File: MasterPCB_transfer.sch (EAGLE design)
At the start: 1070 parts, among them IC1 NCS21911SN2T1G, IC10 LDL1117S33R, IC11 LTC4222CUH#PBF, IC12 LTC4222CUH#PBF, IC13 LTC4222CUH#PBF, IC14 LTC4222CUH#PBF, IC15 LTC4222CUH#PBF, IC16 LTC4222CUH#PBF, IC17 LTC4222CUH#PBF, IC18 LTC4222CUH#PBF, IC19 LTC4222CUH#PBF, IC2 NCS21911SN2T1G, IC20 LTC4222CUH#PBF, IC21 LTC4222CUH#PBF, IC22 LTC4222CUH#PBF, IC23 LTC4222CUH#PBF, IC24 NCS21911SN2T1G, IC25 NCS21911SN2T1G, IC26 NCS21911SN2T1G, IC27 NCS21911SN2T1G, IC28 NCS21911SN2T1G, IC29 NCS21911SN2T1G, IC3 NCS21911SN2T1G, IC30 NCS21911SN2T1G, IC31 ADIS16500AMLZ, IC32 LTC6820IUD#PBF, IC33 CBTL01023GM,115, IC34 MAX889TESA+, IC35 NCS21911SN2T1G, IC36 NCS21911SN2T1G, IC37 NCS21911SN2T1G, IC38 ADS8588HIPM, IC39 NCS21911SN2T1G, IC4 LTC4222CUH#PBF, IC40 NCS21911SN2T1G, IC41 NCS21911SN2T1G, IC42 NCS21911SN2T1G, IC43 NCS21911SN2T1G, IC44 NCS21911SN2T1G, IC45 NCS21911SN2T1G, IC46 NCS21911SN2T1G, IC47 NCS21911SN2T1G, IC48 NCS21911SN2T1G, IC49 NCS21911SN2T1G, IC5 LP38692SDX-5.0_NOPB, IC50 NCS21911SN2T1G, IC51 ADS8588HIPM, IC52 ADS8588HIPM, IC53 NCS21911SN2T1G, IC54 NCS21911SN2T1G, IC55 NCS21911SN2T1G, IC56 NCS21911SN2T1G, IC57 NCS21911SN2T1G, IC58 NCS21911SN2T1G, IC59 NCS21911SN2T1G, IC6 LP38692SDX-5.0_NOPB, IC60 NCS21911SN2T1G, IC61 NCS21911SN2T1G, IC62 NCS21911SN2T1G, IC63 NCS21911SN2T1G, IC64 NCS21911SN2T1G, IC65 NCS21911SN2T1G, IC66 NCS21911SN2T1G, IC67 NCS21911SN2T1G, IC68 NCS21911SN2T1G, IC69 NCS21911SN2T1G, IC7 LDL1117S33R, IC70 NCS21911SN2T1G, IC71 NCS21911SN2T1G, IC72 NCS21911SN2T1G, IC73 NCS21911SN2T1G, IC74 NCS21911SN2T1G, IC75 NCS21911SN2T1G, IC76 NCS21911SN2T1G, IC77 NCS21911SN2T1G, IC78 NCS21911SN2T1G, IC79 NCS21911SN2T1G, IC8 LDL1117S33R, IC9 LP38692SDX-5.0_NOPB, J1 SAMTEC-SMM-104-02-X-DJ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

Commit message: Save point
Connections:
- removed net N$43: J4.18
- removed net N$46: J4.20
- net ISO_SPI_CH_SEL: now also J4.18
- net ISO_SPI_HIGH_Z_SWITCH: now also J4.20
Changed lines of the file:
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@@
 <wire x1="236.22" y1="-17.78" x2="241.3" y2="-17.78" width="0.1524" layer="94"/>
 <wire x1="241.3" y1="-17.78" x2="241.3" y2="-33.02" width="0.1524" layer="94"/>
-<wire x1="241.3" y1="-43.18" x2="236.22" y2="-43.18" width="0.1524" layer="94"/>
+<wire x1="241.3" y1="-38.1" x2="236.22" y2="-38.1" width="0.1524" layer="94"/>
 <text x="243.84" y="-30.48" size="1.778" layer="97">Flash interface</text>
-<wire x1="241.3" y1="-43.18" x2="241.3" y2="-55.88" width="0.1524" layer="94"/>
+<wire x1="241.3" y1="-38.1" x2="241.3" y2="-55.88" width="0.1524" layer="94"/>
 <wire x1="241.3" y1="-55.88" x2="236.22" y2="-55.88" width="0.1524" layer="94"/>
 <text x="243.84" y="-50.8" size="1.778" layer="97">ISO SPI link interface</text>
@@
 </segment>
 </net>
-<net name="N$43" class="0">
+<net name="ISO_SPI_CH_SEL" class="0">
 <segment>
 <pinref part="J4" gate="G$1" pin="18"/>
 <wire x1="205.74" y1="-40.64" x2="203.2" y2="-40.64" width="0.1524" layer="91"/>
-</segment>
-</net>
-<net name="N$46" class="0">
+<label x="208.28" y="-40.64" size="1.778" layer="95"/>
+</segment>
+</net>
+<net name="ISO_SPI_HIGH_Z_SWITCH" class="0">
 <segment>
 <pinref part="J4" gate="G$1" pin="20"/>
 <wire x1="205.74" y1="-43.18" x2="203.2" y2="-43.18" width="0.1524" layer="91"/>
-</segment>
-</net>
+<label x="208.28" y="-43.18" size="1.778" layer="95"/>
+</segment>
+</net>

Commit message: Night check point
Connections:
- removed net 12V: C33.1, C34.1, C35.1, IC1.VDD, IC2.VDD, IC3.VDD
- net 13.5V_BUS: now also C33.1, C34.1, C35.1, IC1.VDD, IC2.VDD, IC3.VDD
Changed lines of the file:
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@@
-</segment>
-</net>
-<net name="12V" class="0">
-<segment>
-<pinref part="IC1" gate="G$1" pin="VDD"/>
-<wire x1="289.56" y1="218.44" x2="294.64" y2="218.44" width="0.1524" layer="91"/>
-<label x="294.64" y="218.44" size="1.778" layer="95"/>
-<pinref part="C33" gate="G$1" pin="1"/>
-<wire x1="294.64" y1="218.44" x2="294.64" y2="215.9" width="0.1524" layer="91"/>
-</segment>
-<segment>
-<pinref part="IC2" gate="G$1" pin="VDD"/>
-<wire x1="289.56" y1="177.8" x2="294.64" y2="177.8" width="0.1524" layer="91"/>
-<label x="294.64" y="177.8" size="1.778" layer="95"/>
-<pinref part="C34" gate="G$1" pin="1"/>
-<wire x1="294.64" y1="177.8" x2="294.64" y2="175.26" width="0.1524" layer="91"/>
-</segment>
-<segment>
-<pinref part="IC3" gate="G$1" pin="VDD"/>
-<wire x1="289.56" y1="137.16" x2="294.64" y2="137.16" width="0.1524" layer="91"/>
-<label x="294.64" y="137.16" size="1.778" layer="95"/>
-<pinref part="C35" gate="G$1" pin="1"/>
-<wire x1="294.64" y1="137.16" x2="294.64" y2="134.62" width="0.1524" layer="91"/>
 </segment>
 </net>
@@
 </segment>
 </net>
+<net name="13.5V_BUS" class="0">
+<segment>
+<pinref part="IC1" gate="G$1" pin="VDD"/>
+<wire x1="289.56" y1="218.44" x2="294.64" y2="218.44" width="0.1524" layer="91"/>
+<label x="294.64" y="218.44" size="1.778" layer="95"/>
+<pinref part="C33" gate="G$1" pin="1"/>
+<wire x1="294.64" y1="218.44" x2="294.64" y2="215.9" width="0.1524" layer="91"/>
+</segment>
+<segment>
+<pinref part="IC2" gate="G$1" pin="VDD"/>
+<wire x1="289.56" y1="177.8" x2="294.64" y2="177.8" width="0.1524" layer="91"/>
+<label x="294.64" y="177.8" size="1.778" layer="95"/>
+<pinref part="C34" gate="G$1" pin="1"/>
+<wire x1="294.64" y1="177.8" x2="294.64" y2="175.26" width="0.1524" layer="91"/>
+</segment>
+<segment>
+<pinref part="IC3" gate="G$1" pin="VDD"/>
+<wire x1="289.56" y1="137.16" x2="294.64" y2="137.16" width="0.1524" layer="91"/>
+<label x="294.64" y="137.16" size="1.778" layer="95"/>
+<pinref part="C35" gate="G$1" pin="1"/>
+<wire x1="294.64" y1="137.16" x2="294.64" y2="134.62" width="0.1524" layer="91"/>
+</segment>
+</net>

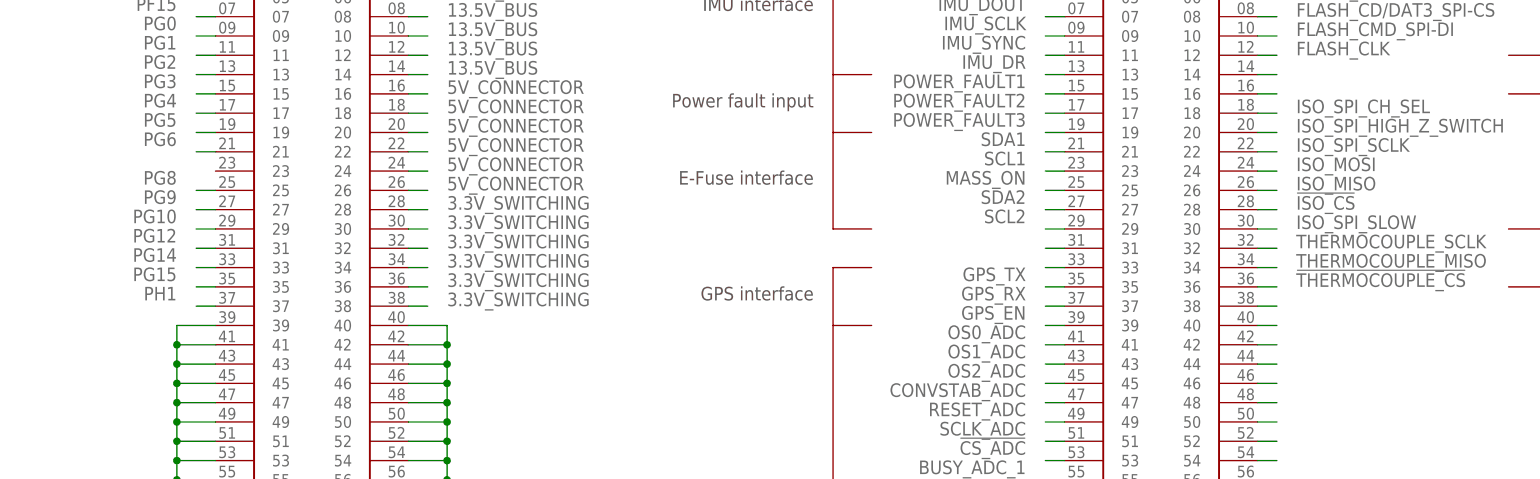
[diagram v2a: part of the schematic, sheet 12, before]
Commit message: Checked warnings on schematic, connected 40G input pin
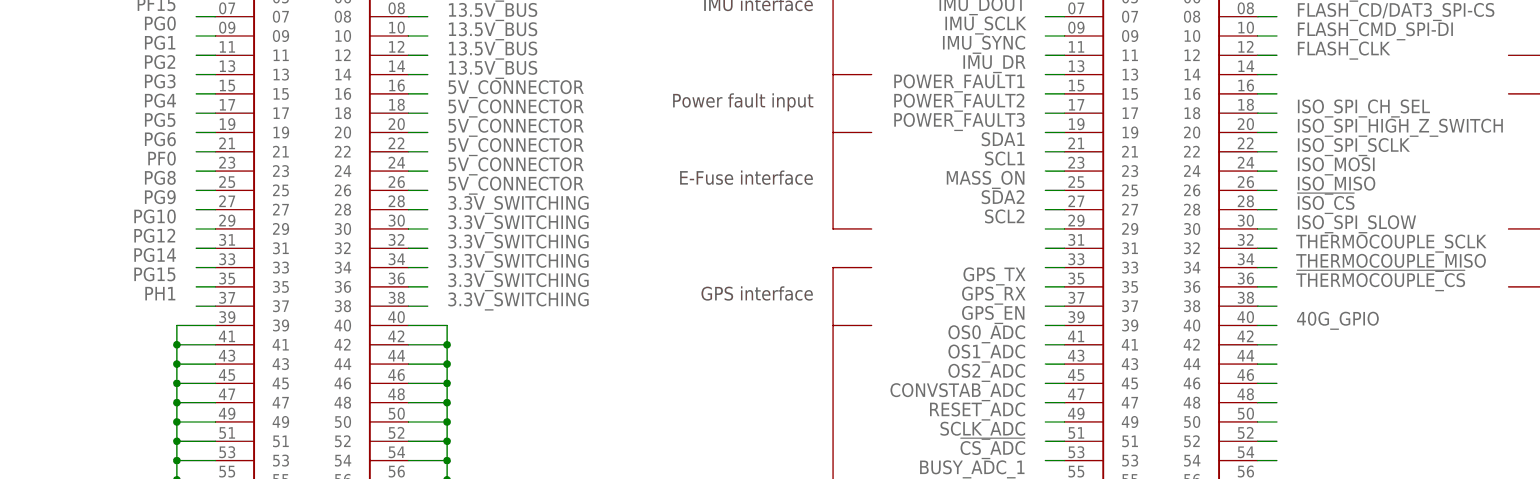
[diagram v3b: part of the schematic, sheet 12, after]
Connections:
- removed net N$159: IC14.ADR0
- removed net N$5: J4.40
- net 40G_GPIO: now also J4.40
- net GND: now also IC14.ADR0
- net PF0: now also J12.23
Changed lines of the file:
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@@
 <part name="GND538" library="supply1" library_urn="urn:adsk.eagle:library:371" deviceset="GND" device=""/>
 <part name="GND539" library="supply1" library_urn="urn:adsk.eagle:library:371" deviceset="GND" device=""/>
-<part name="GND540" library="supply1" library_urn="urn:adsk.eagle:library:371" deviceset="GND" device=""/>
 <part name="GND541" library="supply1" library_urn="urn:adsk.eagle:library:371" deviceset="GND" device=""/>
 <part name="GND542" library="supply1" library_urn="urn:adsk.eagle:library:371" deviceset="GND" device=""/>
@@
 <part name="GND581" library="supply1" library_urn="urn:adsk.eagle:library:371" deviceset="GND" device=""/>
 <part name="GND582" library="supply1" library_urn="urn:adsk.eagle:library:371" deviceset="GND" device=""/>
+<part name="GND540" library="supply1" library_urn="urn:adsk.eagle:library:371" deviceset="GND" device=""/>
 </parts>
 <sheets>
@@
 <attribute name="VALUE" x="853.44" y="320.04" size="1.778" layer="96" rot="R270"/>
 </instance>
-<instance part="GND540" gate="1" x="71.12" y="574.04" smashed="yes" rot="R270">
-<attribute name="VALUE" x="68.58" y="576.58" size="1.778" layer="96" rot="R270"/>
-</instance>
 <instance part="GND541" gate="1" x="71.12" y="817.88" smashed="yes" rot="R270">
 <attribute name="VALUE" x="68.58" y="820.42" size="1.778" layer="96" rot="R270"/>
@@
 <attribute name="VALUE" x="-114.3" y="60.96" size="1.778" layer="96" rot="R90"/>
 </instance>
+<instance part="GND540" gate="1" x="71.12" y="574.04" smashed="yes" rot="R270">
+<attribute name="VALUE" x="68.58" y="576.58" size="1.778" layer="96" rot="R270"/>
+</instance>
 </instances>
 <busses>
@@
 <pinref part="GND580" gate="1" pin="GND"/>
 </segment>
+<segment>
+<pinref part="IC14" gate="G$1" pin="ADR0"/>
+<pinref part="GND540" gate="1" pin="GND"/>
+<wire x1="76.2" y1="574.04" x2="73.66" y2="574.04" width="0.1524" layer="91"/>
+</segment>
 </net>
 <net name="DIFF1_P" class="0">
@@
 </segment>
 </net>
-<net name="N$159" class="0">
-<segment>
-<pinref part="IC14" gate="G$1" pin="ADR0"/>
-<wire x1="76.2" y1="574.04" x2="73.66" y2="574.04" width="0.1524" layer="91"/>
-<pinref part="GND540" gate="1" pin="GND"/>
-</segment>
-</net>
 <net name="N$160" class="0">
 <segment>
@@
 <label x="-5.08" y="33.02" size="1.778" layer="95" rot="R180"/>
 </segment>
+<segment>
+<pinref part="J12" gate="G$1" pin="23"/>
+<wire x1="66.04" y1="-48.26" x2="63.5" y2="-48.26" width="0.1524" layer="91"/>
+<label x="60.96" y="-45.72" size="1.778" layer="95" rot="R180"/>
+</segment>
 </net>
 <net name="PF1" class="0">
@@
 </segment>
 </net>
-<net name="N$5" class="0">
+<net name="40G_GPIO" class="0">
 <segment>
 <wire x1="203.2" y1="-68.58" x2="205.74" y2="-68.58" width="0.1524" layer="91"/>
 <pinref part="J4" gate="G$1" pin="40"/>
+<label x="208.28" y="-68.58" size="1.778" layer="95"/>
 </segment>
 </net>
@@
 </sheet>
 </sheets>
+<errors>
+</errors>
 </schematic>
 </drawing>

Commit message: Adding test points
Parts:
- removed U$6, U$8: THROUGH_HOLE, SamacSys_Parts:THROUGH_HOLE
- added TP10, TP100, TP101, TP102, TP103, TP104, TP105, TP106, TP107, TP108, TP109, TP11, TP110, TP111, TP112, TP113, TP114, TP115, TP116, TP117, TP118, TP119, TP12, TP120, TP121, TP122, TP123, TP124, TP125, TP126, TP127, TP128, TP129, TP13, TP130, TP131, TP132, TP133, TP134, TP135, TP136, TP137, TP138, TP139, TP14, TP140, TP141, TP142, TP143, TP144, TP145, TP146, TP147, TP148, TP149, TP15, TP150, TP151, TP152, TP153, TP154, TP155, TP156, TP157, TP158, TP159, TP16, TP160, TP161, TP162, TP163, TP164, TP17, TP18, TP19, TP2, TP20, TP21, TP22, TP23, TP24, TP25, TP26, TP27, TP28, TP29, TP3, TP30, TP31, TP32, TP33, TP34, TP35, TP36, TP37, TP38, TP39, TP4, TP40, TP41, TP42, TP43, TP44, TP45, TP46, TP47, TP48, TP49, TP5, TP50, TP51, TP52, TP53, TP54, TP55, TP56, TP57, TP58, TP59, TP6, TP60, TP61, TP62, TP63, TP64, TP65, TP66, TP67, TP68, TP69, TP7, TP70, TP71, TP72, TP73, TP74, TP75, TP76, TP77, TP78, TP79, TP8, TP80, TP81, TP82, TP83, TP84, TP85, TP86, TP87, TP88, TP89, TP9, TP90, TP91, TP92, TP93, TP94, TP95, TP96, TP97, TP98, TP99: SMALL_TP, SamacSys_Parts:SMALL_TP
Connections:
- net !CS_ADC: now also TP123.TP
- net !IMU_CS: now also TP100.TP
- net !IMU_RST: now also TP99.TP
- net !ISO_CS: now also TP146.TP
- net !THERMOCOUPLE_CS: now also TP150.TP
- net 40G_GPIO: now also TP153.TP
- net BUSY_ADC_1: now also TP124.TP
- net BUSY_ADC_2: now also TP128.TP
- net BUSY_ADC_3: now also TP132.TP
- net CONVSTAB_ADC: now also TP120.TP
- net DOUTA_ADC_1: now also TP127.TP
- net DOUTA_ADC_2: now also TP131.TP
- net DOUTA_ADC_3: now also TP135.TP
- net DOUTB_ADC_1: now also TP126.TP
- net DOUTB_ADC_2: now also TP130.TP
- net DOUTB_ADC_3: now also TP134.TP
- net D_SENSE1: now also TP158.TP
- net D_SENSE2: now also TP157.TP
- net D_SENSE3: now also TP159.TP
- net D_SENSE4: now also TP161.TP
- net D_SENSE5: now also TP160.TP
- net D_SENSE6: now also TP162.TP
- net D_SENSE7: now also TP164.TP
- net D_SENSE8: now also TP163.TP
- net FIRSTDATA_ADC_1: now also TP125.TP
- net FIRSTDATA_ADC_2: now also TP129.TP
- net FIRSTDATA_ADC_3: now also TP133.TP
- net FLASH_CD/DAT3_SPI-CS: now also TP138.TP
- net FLASH_CLK: now also TP140.TP
- net FLASH_CMD_SPI-DI: now also TP141.TP
- net FLASH_DAT0_SPI-DO: now also TP137.TP
- net FLASH_DAT1: now also TP136.TP
- net FLASH_DAT2: now also TP139.TP
- net GPS_EN: now also TP116.TP
- net GPS_RX: now also TP115.TP
- net GPS_TX: now also TP114.TP
- net IMU_DIN: now also TP101.TP
- net IMU_DOUT: now also TP102.TP
- net IMU_DR: now also TP105.TP
- net IMU_SCLK: now also TP103.TP
- net IMU_SYNC: now also TP104.TP
- net ISO_MISO: now also TP147.TP
- net ISO_MOSI: now also TP144.TP
- net ISO_SPI_CH_SEL: now also TP143.TP
- net ISO_SPI_HIGH_Z_SWITCH: now also TP142.TP
- net ISO_SPI_SCLK: now also TP145.TP
- net ISO_SPI_SLOW: now also TP149.TP
- net LED_OUT1: now also TP154.TP
- net LED_OUT2: now also TP155.TP
- net LED_OUT3: now also TP152.TP
- net MASS_ON: now also TP111.TP
- net OS0_ADC: now also TP117.TP
- net OS1_ADC: now also TP118.TP
- net OS2_ADC: now also TP119.TP
- net PA0: no longer J14.01
- net PA10: now also TP8.TP
- net PA11: now also TP9.TP
- net PA12: now also TP10.TP
- net PA13: now also TP11.TP
- net PA14: now also TP12.TP
- net PA15: now also TP13.TP
- net PA3: now also TP2.TP
- net PA4: now also TP3.TP
- net PA5: now also TP4.TP
- net PA6: now also TP5.TP
- net PA8: now also TP6.TP
- net PA9: now also TP7.TP
- net PB0: now also TP14.TP
- net PB1: now also TP15.TP
- net PB10: now also TP36.TP
- net PB11: now also TP35.TP
- net PB12: now also TP34.TP
- net PB14: now also TP33.TP
- net PB15: now also TP32.TP
- net PB2: now also TP16.TP
- net PB3: now also TP17.TP
- net PB4: now also TP18.TP
- net PB5: now also TP19.TP
- net PB6: now also TP20.TP
- net PB7: now also TP39.TP
- net PB8: now also TP38.TP
- net PB9: now also TP37.TP
- net PC0: now also TP31.TP
- net PC10: now also TP24.TP
- net PC11: now also TP23.TP
- net PC12: now also TP22.TP
- net PC13: now also TP21.TP
- net PC2: now also TP30.TP
- net PC3: now also TP29.TP
- net PC6: now also TP28.TP
- net PC7: now also TP27.TP
- net PC8: now also TP26.TP
- net PC9: now also TP25.TP
- net PD0: now also TP40.TP
- net PD1: now also TP41.TP
- net PD11: now also TP48.TP
- net PD12: now also TP49.TP
- net PD13: now also TP50.TP
- net PD14: now also TP51.TP
- net PD15: now also TP52.TP
- net PD2: now also TP42.TP
- net PD3: now also TP43.TP
- net PD4: now also TP44.TP
- net PD5: now also TP45.TP
- net PD6: now also TP46.TP
- net PD7: now also TP47.TP
- net PE0: now also TP53.TP
- net PE1: now also TP54.TP
- net PE10: now also TP76.TP
- net PE11: now also TP75.TP
- net PE12: now also TP74.TP
- net PE13: now also TP73.TP
- net PE14: now also TP72.TP
- net PE15: now also TP71.TP
- net PE2: now also TP55.TP
- net PE3: now also TP56.TP
- net PE4: now also TP57.TP
- net PE5: now also TP58.TP
- net PE6: now also TP59.TP
- net PE7: now also TP79.TP
- net PE8: now also TP78.TP
- net PE9: now also TP77.TP
- net PF0: now also TP91.TP
- net PF1: now also TP70.TP
- net PF10: now also TP61.TP
- net PF11: now also TP60.TP
- net PF12: now also TP80.TP
- net PF13: now also TP81.TP
- net PF14: now also TP82.TP
- net PF15: now also TP83.TP
- net PF2: now also TP69.TP
- net PF3: now also TP68.TP
- net PF4: now also TP67.TP
- net PF5: now also TP66.TP
- net PF6: now also TP65.TP
- net PF7: now also TP64.TP
- net PF8: now also TP63.TP
- net PF9: now also TP62.TP
- net PG0: now also TP84.TP
- net PG1: now also TP85.TP
- net PG10: now also TP94.TP
- net PG12: now also TP95.TP
- net PG14: now also TP96.TP
- net PG15: now also TP97.TP
- net PG2: now also TP86.TP
- net PG3: now also TP87.TP
- net PG4: now also TP88.TP
- net PG5: now also TP89.TP
- net PG6: now also TP90.TP
- net PG8: now also TP92.TP
- net PG9: now also TP93.TP
- net PH1: now also TP98.TP
- net POWER_FAULT1: now also TP106.TP
- net POWER_FAULT2: now also TP107.TP
- net POWER_FAULT3: now also TP108.TP
- net P_LED: now also TP156.TP
- net RESET_ADC: now also TP121.TP
- net SCL1: now also TP110.TP
- net SCL2: now also TP113.TP
- net SCLK_ADC: now also TP122.TP
- net SDA1: now also TP109.TP
- net SDA2: now also TP112.TP
- net THERMOCOUPLE_MISO: now also TP151.TP
- net THERMOCOUPLE_SCLK: now also TP148.TP
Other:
- moved on the sheet: J12, J4

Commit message: Labels
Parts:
- renumbered TP10 to PA12, TP100 to !IMU_CS, TP101 to IMU_DIN, TP102 to IMU_DOUT, TP103 to IMU_SCLK, TP104 to IMU_SYNC, TP105 to IMU_DR, TP106 to P_FAULT1, TP107 to P_FAULT2, TP108 to P_FAULT3, TP109 to SDA1, TP11 to PA13, TP110 to SCL1, TP111 to MASS_ON, TP112 to SDA2, TP113 to SCL2, TP114 to GPS_TX, TP115 to GPS_RX, TP116 to GPS_EN, TP117 to OS0_ADC, TP118 to OS1_ADC, TP119 to OS2_ADC, TP12 to PA14, TP120 to CONVAB_ADC, TP121 to RST_ADC, TP122 to SCLK_ADC, TP123 to !CS_ADC, TP124 to BUSY_ADC_1, TP125 to FSTD_ADC_1, TP126 to DOUTB_ADC_1, TP127 to DOUTA_ADC_1, TP128 to BUSY_ADC_2, TP129 to FSTD_ADC_2, TP13 to PA15, TP130 to DOUTB_ADC_2, TP131 to DOUTA_ADC_2, TP132 to BUSY_ADC_3, TP133 to FSTD_ADC_3, TP134 to DOUTB_ADC_3, TP135 to DOUTA_ADC_3, TP136 to DAT1, TP137 to DAT_SPI-DO, TP138 to CD/DAT3_SPI-CS, TP139 to DAT2, TP14 to PB0, TP140 to CLK, TP141 to CMD_SPI-DI, TP142 to ISO_SPI_HZ_SW, TP143 to ISO_SPI_CH_SEL, TP144 to ISO_MOSI, TP145 to ISO_SPI_SCLK, TP146 to !ISO_CS, TP147 to ISO_MISO, TP148 to TEMP_SCLK, TP149 to ISO_SPI_SLOW, TP15 to PB1, TP150 to !TEMP_CS, TP151 to TEMP_MISO, TP152 to LED_3, TP153 to 40G_GPIO, TP154 to LED_1, TP155 to LED_2, TP156 to LED_P, TP157 to DIN2, TP158 to DIN1, TP159 to DIN3, TP16 to PB2, TP160 to DIN5, TP161 to DIN4, TP162 to DIN6, TP163 to DIN8, TP164 to DIN7, TP17 to PB3, TP18 to PB4, TP19 to PB5, TP2 to PA3, TP20 to PB6, TP21 to PC13, TP22 to PC12, TP23 to PC11, TP24 to PC10, TP25 to PC9, TP26 to PC8, TP27 to PC7, TP28 to PC6, TP29 to PC3, TP3 to PA4, TP30 to PC2, TP31 to PC0, TP32 to PB15, TP33 to PB14, TP34 to PB12, TP35 to PB11, TP36 to PB10, TP37 to PB9, TP38 to PB8, TP39 to PB7, TP4 to PA5, TP40 to PD0, TP41 to PD1, TP42 to PD2, TP43 to PD3, TP44 to PD4, TP45 to PD5, TP46 to PD6, TP47 to PD7, TP48 to PD11, TP49 to PD12, TP5 to PA6, TP50 to PD13, TP51 to PD14, TP52 to PD15, TP53 to PE0, TP54 to PE1, TP55 to PE2, TP56 to PE3, TP57 to PE4, TP58 to PE5, TP59 to PE6, TP6 to PA8, TP60 to PF11, TP61 to PF10, TP62 to PF9, TP63 to PF8, TP64 to PF7, TP65 to PF6, TP66 to PF5, TP67 to PF4, TP68 to PF3, TP69 to PF2, TP7 to PA9, TP70 to PF1, TP71 to PE15, TP72 to PE14, TP73 to PE13, TP74 to PE12, TP75 to PE11, TP76 to PE10, TP77 to PE9, TP78 to PE8, TP79 to PE7, TP8 to PA10, TP80 to PF12, TP81 to PF13, TP82 to PF14, TP83 to PF15, TP84 to PG0, TP85 to PG1, TP86 to PG2, TP87 to PG3, TP88 to PG4, TP89 to PG5, TP9 to PA11, TP90 to PG6, TP91 to PF0, TP92 to PG8, TP93 to PG9, TP94 to PG10, TP95 to PG12, TP96 to PG14, TP97 to PG15, TP98 to PH1, TP99 to !IMU_RST

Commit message: added new LED voltage clamps
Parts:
- added LED100, LED101, LED102, LED103, LED104, LED105, LED106, LED107, LED108, LED109, LED110, LED111, LED112, LED113, LED114, LED97, LED98, LED99: ASMT-URB4-YU802, SamacSys_Parts:ASMT-URB4-YU802
- added R117, R118, R119, R120, R121, R122, R123, R124, R57, R58, R65, R66, R67, R68, R69, R70, R71, R72: ERJ-PA3D1400V, SamacSys_Parts:ERJ-PA3D1400V
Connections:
- new net ADIN1_0IN: D9.K, J5.11, R65.2
- new net ADIN1_1IN: D63.K, J5.21, R67.2
- new net ADIN1_2IN: D69.K, J5.31, R69.2
- new net ADIN1_3IN: D15.K, J6.41, R71.2
- new net ADIN1_4IN: D21.K, J6.51, R117.2
- new net ADIN1_5IN: D51.K, J6.61, R119.2
- new net ADIN1_6IN: D57.K, J6.71, R121.2
- new net ADIN1_7IN: D27.K, J6.01, R123.2
- new net ADIN1_IN: D3.K, J5.01, R57.2
- new net ADIN2_0IN: D12.K, J5.16, R66.2
- new net ADIN2_1IN: D66.K, J5.26, R68.2
- new net ADIN2_2IN: D72.K, J5.36, R70.2
- new net ADIN2_3IN: D18.K, J6.46, R72.2
- new net ADIN2_4IN: D24.K, J6.56, R118.2
- new net ADIN2_5IN: D54.K, J6.66, R120.2
- new net ADIN2_6IN: D60.K, J6.76, R122.2
- new net ADIN2_7IN: D30.K, J6.06, R124.2
- new net ADIN2_IN: D6.K, J5.06, R58.2
- net ADIN1_: now also LED97.A, R57.1; no longer D3.K, J5.01
- net ADIN1_0: now also LED99.A, R65.1; no longer D9.K, J5.11
- net ADIN1_1: now also LED101.A, R67.1; no longer D63.K, J5.21
- net ADIN1_2: now also LED103.A, R69.1; no longer D69.K, J5.31
- net ADIN1_3: now also LED105.A, R71.1; no longer D15.K, J6.41
- net ADIN1_4: now also LED107.A, R117.1; no longer D21.K, J6.51
- net ADIN1_5: now also LED109.A, R119.1; no longer D51.K, J6.61
- net ADIN1_6: now also LED111.A, R121.1; no longer D57.K, J6.71
- net ADIN1_7: now also LED113.A, R123.1; no longer D27.K, J6.01
- net ADIN2_: now also LED98.A, R58.1; no longer D6.K, J5.06
- net ADIN2_0: now also LED100.A, R66.1; no longer D12.K, J5.16
- net ADIN2_1: now also LED102.A, R68.1; no longer D66.K, J5.26
- net ADIN2_2: now also LED104.A, R70.1; no longer D72.K, J5.36
- net ADIN2_3: now also LED106.A, R72.1; no longer D18.K, J6.46
- net ADIN2_4: now also LED108.A, R118.1; no longer D24.K, J6.56
- net ADIN2_5: now also LED110.A, R120.1; no longer D54.K, J6.66
- net ADIN2_6: now also LED112.A, R122.1; no longer D60.K, J6.76
- net ADIN2_7: now also LED114.A, R124.1; no longer D30.K, J6.06
- net GND: now also LED100.K, LED101.K, LED102.K, LED103.K, LED104.K, LED105.K, LED106.K, LED107.K, LED108.K, LED109.K, LED110.K, LED111.K, LED112.K, LED113.K, LED114.K, LED97.K, LED98.K, LED99.K
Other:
- note added: "ADIN input voltage clamp and indicator"

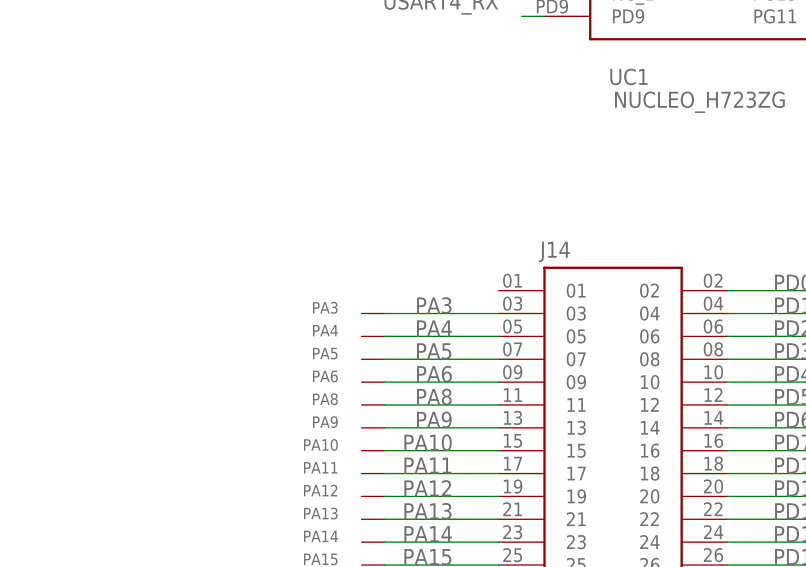
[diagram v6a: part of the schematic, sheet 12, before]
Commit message: Need to add remaining logos and text
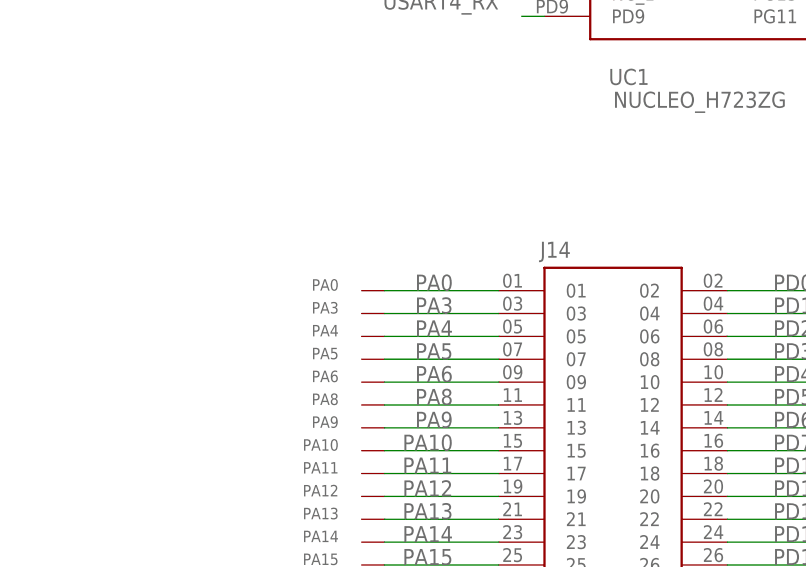
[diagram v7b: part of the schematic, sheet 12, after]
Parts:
- added PA0: SMALL_TP, SamacSys_Parts:SMALL_TP
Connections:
- net PA0: now also J14.01, PA0.TP
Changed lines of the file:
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@@
 <part name="R124" library="SamacSys_Parts" library_urn="urn:adsk.eagle:library:31941355" deviceset="ERJ-PA3D1400V" device="" package3d_urn="urn:adsk.eagle:package:35457111/2"/>
 <part name="GND600" library="supply1" library_urn="urn:adsk.eagle:library:371" deviceset="GND" device=""/>
+<part name="PA0" library="SamacSys_Parts" library_urn="urn:adsk.eagle:library:31941355" deviceset="SMALL_TP" device="" package3d_urn="urn:adsk.eagle:package:35450068/4"/>
 </parts>
 <sheets>
@@
 <attribute name="NAME" x="279.4" y="-68.58" size="1.27" layer="95"/>
 </instance>
+<instance part="PA0" gate="G$1" x="-15.24" y="-20.32" smashed="yes" rot="R90">
+<attribute name="NAME" x="-20.32" y="-20.32" size="1.27" layer="95" rot="MR0"/>
+</instance>
 </instances>
 <busses>
@@
 <label x="45.72" y="63.5" size="1.778" layer="95"/>
 </segment>
+<segment>
+<pinref part="J14" gate="G$1" pin="01"/>
+<wire x1="-2.54" y1="-20.32" x2="-15.24" y2="-20.32" width="0.1524" layer="91"/>
+<pinref part="PA0" gate="G$1" pin="TP"/>
+<label x="-7.62" y="-20.32" size="1.778" layer="95" rot="MR0"/>
+</segment>
 </net>
